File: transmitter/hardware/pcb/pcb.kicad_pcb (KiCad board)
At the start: 2 copper layers, 192.5 x 47 mm, 92 parts, among them M101 MT3608_Modul, P101 TestPoint_Alt, P102 TestPoint_Alt, P103 TestPoint_Alt, P104 TestPoint_Alt, P105 TestPoint_Alt, P106 TestPoint_Alt, P107 TestPoint_Alt, P108 TestPoint_Alt, P109 TestPoint_Alt, P110 TestPoint_Alt, P111 TestPoint_Alt, P112 TestPoint_Alt, P113 TestPoint_Alt, P114 TestPoint_Alt, P115 TestPoint_Alt, P116 TestPoint_Alt, P117 TestPoint_Alt, P118 TestPoint_Alt, P119 TestPoint_Alt, P120 TestPoint_Alt, P121 TestPoint_Alt, P122 TestPoint_Alt, P123 TestPoint_Alt, P124 TestPoint_Alt, P125 TestPoint_Alt, P126 TestPoint_Alt, P127 TestPoint_Alt, P128 TestPoint_Alt, P129 TestPoint_Alt, P130 TestPoint_Alt, P131 TestPoint_Alt, P132 TestPoint_Alt, P133 TestPoint_Alt, P134 TestPoint_Alt, P135 TestPoint_Alt, P136 TestPoint_Alt, P137 TestPoint_Alt, P138 TestPoint_Alt, P139 TestPoint_Alt, P140 TestPoint_Alt, P141 TestPoint_Alt, Q101 BC847, SW101 POWER, SW102 ~RST, X101 power, X102 Display, X103 UART, X104 gimbal_left_h, X105 gimbal_left_v, X106 gimbal_right_h, X107 gimbal_right_v, X108 SW1, X109 SW2, X110 SW3, X111 SW4, X112 SW5, X113 SW6, X114 SW7, X115 SW8, X116 SW1, X117 SW2, X118 SW3, X119 SW4, X120 SW5, X121 SW6, X122 SW7, X123 SW8

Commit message: WIP
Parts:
- removed RN101, RN102: 1k, Resistor_THT:R_Array_SIP9
- removed X110, X118: SW3, Connector_PinHeader_2.54mm:PinHeader_1x02_P2.54mm_Vertical
- removed X111, X119: SW4, Connector_PinHeader_2.54mm:PinHeader_1x02_P2.54mm_Vertical
- removed X112, X120: SW5, Connector_PinHeader_2.54mm:PinHeader_1x02_P2.54mm_Vertical
- removed X113, X121: SW6, Connector_PinHeader_2.54mm:PinHeader_1x02_P2.54mm_Vertical
- removed X114, X122: SW7, Connector_PinHeader_2.54mm:PinHeader_1x02_P2.54mm_Vertical
- removed X115, X123: SW8, Connector_PinHeader_2.54mm:PinHeader_1x02_P2.54mm_Vertical
- removed X116: SW1, Connector_PinHeader_2.54mm:PinHeader_1x02_P2.54mm_Vertical
- removed X117: SW2, Connector_PinHeader_2.54mm:PinHeader_1x02_P2.54mm_Vertical
- added R104: 1k, Resistor_SMD:R_0603_1608Metric, B.Cu at (128.6, 88.2)
- added R105: 1k, Resistor_SMD:R_0603_1608Metric, B.Cu at (108.3, 88.2)
- added R106: 1k, Resistor_SMD:R_0603_1608Metric, B.Cu at (126.1, 88.2)
- added R107: 1k, Resistor_SMD:R_0603_1608Metric, B.Cu at (105.7, 88.2)
- added R108: 1k, Resistor_SMD:R_0603_1608Metric, B.Cu at (123.5, 88.2)
- added R109: 1k, Resistor_SMD:R_0603_1608Metric, B.Cu at (103.2, 88.2)
- added R110: 1k, Resistor_SMD:R_0603_1608Metric, B.Cu at (121.0, 88.2)
- added R111: 1k, Resistor_SMD:R_0603_1608Metric, B.Cu at (100.7, 88.2)
- added R112: 1k, Resistor_SMD:R_0603_1608Metric, B.Cu at (118.4, 88.2)
- added R113: 1k, Resistor_SMD:R_0603_1608Metric, B.Cu at (98.1, 88.2)
- added R114: 1k, Resistor_SMD:R_0603_1608Metric, B.Cu at (115.9, 88.2)
- added R115: 1k, Resistor_SMD:R_0603_1608Metric, B.Cu at (95.6, 88.2)
- added R116: 1k, Resistor_SMD:R_0603_1608Metric, B.Cu at (113.4, 88.2)
- added R117: 1k, Resistor_SMD:R_0603_1608Metric, B.Cu at (93.0, 88.2)
- added R118: 1k, Resistor_SMD:R_0603_1608Metric, B.Cu at (110.8, 88.2)
- added R119: 1k, Resistor_SMD:R_0603_1608Metric, B.Cu at (90.5, 88.2)
- X108: value SW1 -> switches_1; footprint Connector_PinHeader_2.54mm:PinHeader_1x02_P2.54mm_Vertical -> Connector_PinHeader_2.54mm:PinHeader_2x08_P2.54mm_Vertical
- X109: value SW2 -> switches_2; footprint Connector_PinHeader_2.54mm:PinHeader_1x02_P2.54mm_Vertical -> Connector_PinHeader_2.54mm:PinHeader_2x08_P2.54mm_Vertical
- moved X108 88.7 mm to (128.6, 83.1), turned to 270 degrees
- moved P132 86.3 mm to (128.0, 93.3), turned to 270 degrees
- moved P124 85.4 mm to (128.6, 89.5), turned to 90 degrees
- moved P125 81.4 mm to (126.1, 89.5), turned to 90 degrees
- moved S104 77.7 mm to (121.6, 95.8), turned to 90 degrees
- moved P126 77.3 mm to (123.5, 89.5), turned to 90 degrees
- moved X109 75.0 mm to (108.3, 83.1), turned to 270 degrees
- moved P127 73.3 mm to (121.0, 89.5), turned to 90 degrees
- moved P128 69.2 mm to (118.4, 89.5), turned to 90 degrees
- moved C111 68.7 mm to (115.3, 95.8), turned to 270 degrees
- moved P129 65.1 mm to (115.9, 89.5), turned to 90 degrees
- moved P141 63.8 mm to (90.5, 89.5), turned to 270 degrees
- moved P140 61.3 mm to (95.6, 89.5), turned to 90 degrees
- moved P130 61.1 mm to (113.4, 89.5), turned to 90 degrees
- moved R103 59.7 mm to (91.1, 93.9), turned to 0 degrees
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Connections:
- P134 pad 1: /SW10 -> /SW11
- P135 pad 1: /SW11 -> /SW13
- P137 pad 1: /SW12 -> /SW15
- P138 pad 1: /SW13 -> /SW10
- P139 pad 1: /SW14 -> /SW12
- P140 pad 1: /SW15 -> /SW14
- X108 pad 1: /SW1 -> GND
- X108 pad 2: GND -> /SW1
- X109 pad 1: /SW2 -> GND
- X109 pad 2: GND -> /SW9

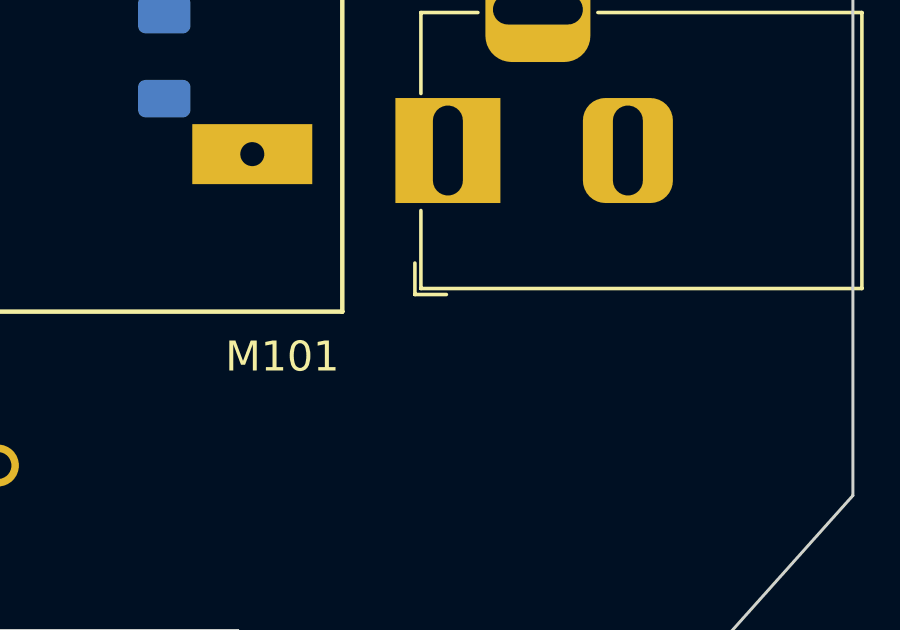
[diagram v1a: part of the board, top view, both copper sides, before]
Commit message: add dc jack for charger connection
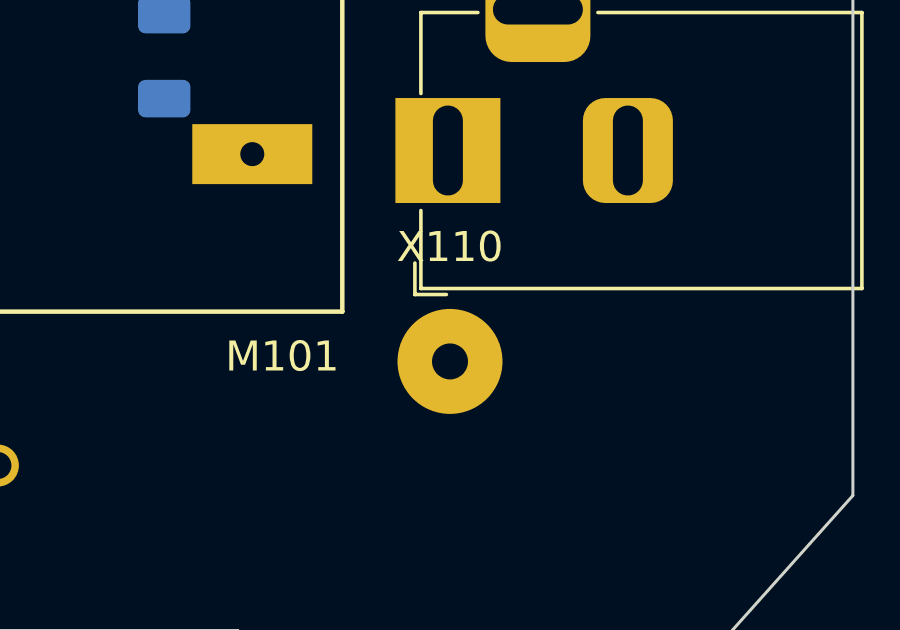
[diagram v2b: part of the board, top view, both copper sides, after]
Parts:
- added X110: chrg_out, Connector_Wire:SolderWirePad_1x01_Drill1.2mm, F.Cu at (216.2, 146.6)
- XA02: value Charger -> charge
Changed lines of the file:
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@@
     (tracks 0)
     (zones 0)
-    (modules 92)
+    (modules 93)
     (nets 51)
   )
@@
     (34 B.Paste user)
     (35 F.Paste user)
-    (36 B.SilkS user hide)
-    (37 F.SilkS user hide)
+    (36 B.SilkS user)
+    (37 F.SilkS user)
     (38 B.Mask user)
     (39 F.Mask user)
@@
     (add_net "Net-(SW101-Pad3)")
   )
+  (module Connector_Wire:SolderWirePad_1x01_Drill1.2mm (layer F.Cu)
+    (at 216.23 146.647)
+    (descr "Wire solder connection")
+    (tags connector)
+    (attr virtual)
+    (fp_text reference X110 (at 0 -3.81) (layer F.SilkS)
+      (effects (font (size 1 1) (thickness 0.15)))
+    )
+    (fp_text value chrg_out (at 0 3.175) (layer F.Fab)
+      (effects (font (size 1 1) (thickness 0.15)))
+    )
+    (fp_text user %R (at 0 0) (layer F.Fab)
+      (effects (font (size 1 1) (thickness 0.15)))
+    )
+    (fp_line (start -2.25 -2.25) (end 2.25 -2.25) (layer F.CrtYd) (width 0.05))
+    (fp_line (start -2.25 -2.25) (end -2.25 2.25) (layer F.CrtYd) (width 0.05))
+    (fp_line (start 2.25 2.25) (end 2.25 -2.25) (layer F.CrtYd) (width 0.05))
+    (fp_line (start 2.25 2.25) (end -2.25 2.25) (layer F.CrtYd) (width 0.05))
+    (pad 1 thru_hole circle (at 0 0) (size 3.50012 3.50012) (drill 1.19888) (layers *.Cu *.Mask)
+      (net 12 +5C))
+  )
   (module Connector_PinHeader_2.54mm:PinHeader_2x08_P2.54mm_Vertical (layer F.Cu)
     (at 108.28 83.147 270)
@@
       (effects (font (size 1 1) (thickness 0.15)))
     )
-    (fp_text value Charger (at -6.2 -5.5 180) (layer F.Fab)
+    (fp_text value charge (at -6.2 -5.5 180) (layer F.Fab)
       (effects (font (size 1 1) (thickness 0.15)))
     )
